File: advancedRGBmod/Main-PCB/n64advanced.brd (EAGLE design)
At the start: 64.5 x 37.7 mm, 112 parts, among them J6 UPS, U1 10CL010YE144, U2 ADV7125/ADV7123, U4 74LVC3G17, U5 S25FLXXXSO8-DUAL, U6 TLV70012DDC, U7 TLV70025DDC

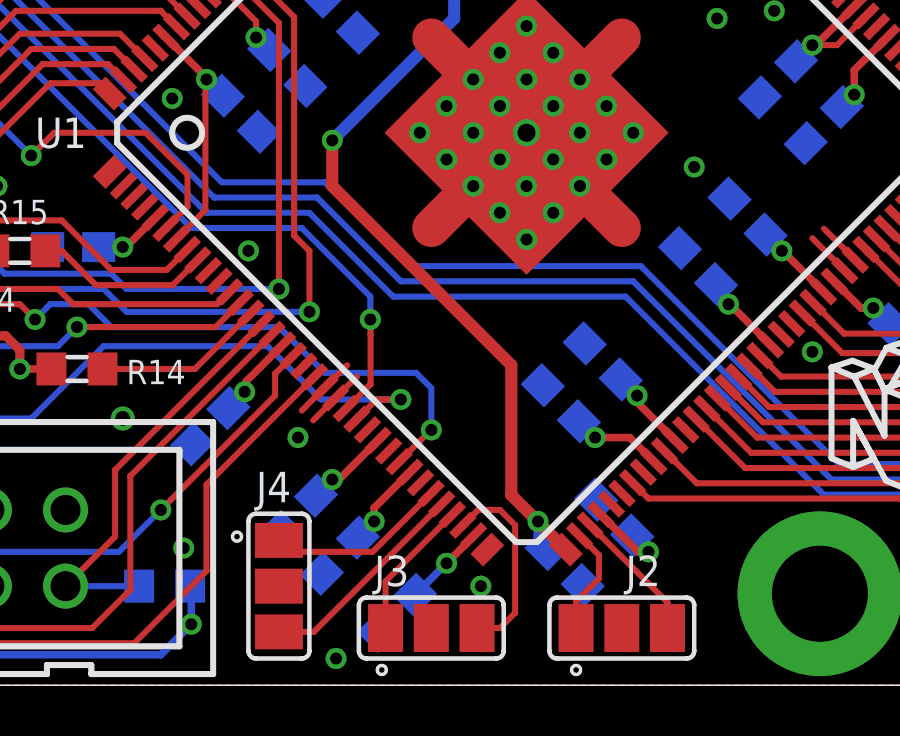
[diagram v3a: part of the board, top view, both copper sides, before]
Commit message: important DRC error fix in PCB design! If you ordered version N64A_20171017 - like I did -, you can unfortunately throw them away :(. There was a design error in the board such that there is a short in an internal plane between VCCDPLL (1.2V) and VCCA (2.5V), which is not easy to fix (fix would need some trace cuts and rewiring)
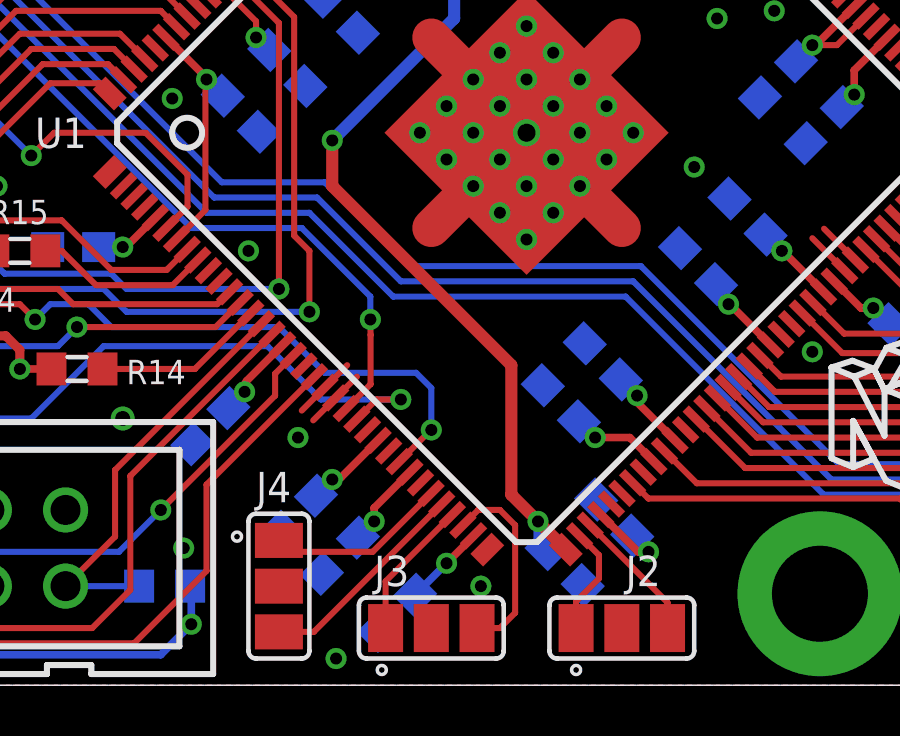
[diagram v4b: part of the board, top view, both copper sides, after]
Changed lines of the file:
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@@
 <layer number="13" name="Route13" color="4" fill="5" visible="no" active="no"/>
 <layer number="14" name="Route14" color="1" fill="6" visible="no" active="no"/>
-<layer number="15" name="Route15" color="4" fill="6" visible="no" active="yes"/>
+<layer number="15" name="Route15" color="4" fill="6" visible="yes" active="yes"/>
 <layer number="16" name="Bottom" color="1" fill="1" visible="yes" active="yes"/>
 <layer number="17" name="Pads" color="2" fill="1" visible="yes" active="yes"/>
@@
 <wire x1="28.702" y1="33.401" x2="28.702" y2="22.225" width="0.4064" layer="16"/>
 <via x="24.638" y="18.161" extent="1-16" drill="0.4"/>
-<wire x1="30.607" y1="6.336496875" x2="32.423146875" y2="4.52035" width="0.4064" layer="1"/>
 <via x="31.496" y="5.461" extent="1-16" drill="0.4"/>
-<wire x1="32.56365" y1="4.52035" x2="32.423146875" y2="4.52035" width="0.254" layer="1"/>
+<wire x1="32.423146875" y1="4.52035" x2="32.56365" y2="4.52035" width="0.254" layer="1"/>
 <wire x1="28.702" y1="22.225" x2="24.638" y2="18.161" width="0.4064" layer="16"/>
 <wire x1="24.638" y1="18.161" x2="24.638" y2="16.637" width="0.4064" layer="1"/>
 <contactref element="U1" pad="37"/>
 <contactref element="U1" pad="109"/>
-<wire x1="24.638" y1="16.637" x2="30.607" y2="10.668" width="0.4064" layer="1"/>
-<wire x1="30.607" y1="10.668" x2="30.607" y2="6.336496875" width="0.4064" layer="1"/>
+<wire x1="30.607" y1="10.668" x2="24.638" y2="16.637" width="0.4064" layer="1"/>
 <wire x1="31.783959375" y1="4.538040625" x2="31.496" y2="4.826" width="0.3048" layer="16"/>
 <wire x1="31.496" y1="4.826" x2="31.496" y2="5.461" width="0.3048" layer="16"/>
-<wire x1="31.783959375" y1="4.538040625" x2="32.423146875" y2="4.52035" width="0" layer="19" extent="1-16"/>
+<wire x1="30.607" y1="6.35" x2="31.496" y2="5.461" width="0.4064" layer="1"/>
+<wire x1="30.607" y1="6.35" x2="30.607" y2="10.668" width="0.4064" layer="1"/>
+<wire x1="31.496" y1="5.461" x2="32.423146875" y2="4.533853125" width="0.4064" layer="1"/>
+<wire x1="32.423146875" y1="4.533853125" x2="32.423146875" y2="4.52035" width="0.4064" layer="1"/>
 </signal>
 <signal name="VCCIO">
@@
 <wire x1="28.448" y1="4.064" x2="27.051" y2="2.667" width="0.254" layer="15"/>
 <wire x1="45.212" y1="21.336" x2="45.212" y2="12.7" width="0.4064" layer="15"/>
-<wire x1="45.212" y1="12.7" x2="38.354" y2="5.842" width="0.4064" layer="15"/>
-<wire x1="38.354" y1="5.842" x2="30.226" y2="5.842" width="0.4064" layer="15"/>
-<wire x1="30.226" y1="5.842" x2="28.448" y2="4.064" width="0.4064" layer="15"/>
+<wire x1="45.212" y1="12.7" x2="38.989" y2="6.477" width="0.4064" layer="15"/>
+<wire x1="38.989" y1="6.477" x2="30.861" y2="6.477" width="0.4064" layer="15"/>
+<wire x1="30.861" y1="6.477" x2="28.448" y2="4.064" width="0.4064" layer="15"/>
 <wire x1="27.051" y1="2.667" x2="20.574" y2="2.667" width="0.254" layer="15"/>
 <wire x1="20.574" y1="2.667" x2="19.939" y2="2.032" width="0.254" layer="15"/>

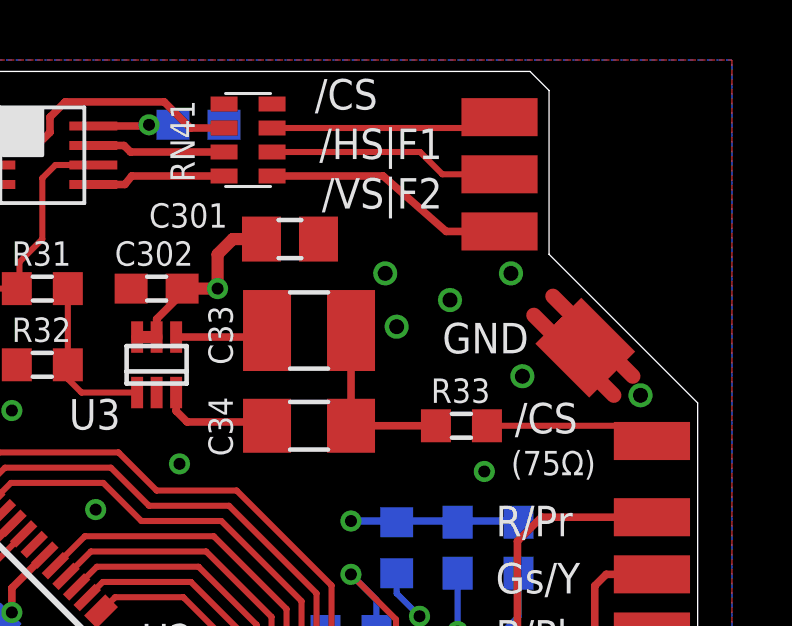
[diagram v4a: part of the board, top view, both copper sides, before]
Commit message: remove separate eagle 7.x version
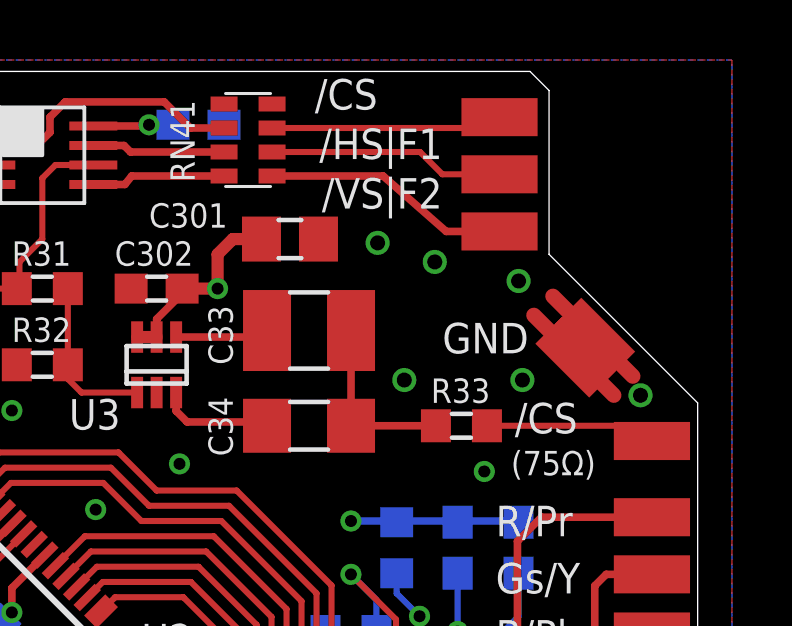
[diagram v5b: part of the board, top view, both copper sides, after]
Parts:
- moved U$1 1.63 mm to (59.7, 27.9)
- moved U$2 1.27 mm to (47.2, 26.9)
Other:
- board text added: "N64A_20171019"
- board text removed: "N64A_20171017"
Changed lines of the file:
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@@
 <circle x="32.766" y="0.508" radius="0.05679375" width="0.3048" layer="25"/>
 <circle x="29.464" y="37.211" radius="0.05679375" width="0.3048" layer="25"/>
-<text x="10.668" y="1.27" size="1.016" layer="26" font="vector" ratio="12" rot="MR0" align="center">N64A_20171017</text>
+<text x="10.668" y="1.27" size="1.016" layer="26" font="vector" ratio="12" rot="MR0" align="center">N64A_20171019</text>
 <wire x1="11.303" y1="30.861" x2="11.303" y2="33.909" width="0.1524" layer="25"/>
 <wire x1="11.303" y1="33.909" x2="12.573" y2="35.179" width="0.1524" layer="25"/>
@@
 <attribute name="OC_NEWARK" value="unknown" x="59.69" y="15.113" size="1.778" layer="27" rot="R270" display="off"/>
 </element>
-<element name="U8" library="crystal-geyer_V1_0" library_urn="urn:adsk.eagle:library:203" package="3.2X2.5_KXO-V96" package3d_urn="urn:adsk.eagle:package:11941/1" value="" x="7.62" y="10.795" smashed="yes" rot="R180">
+<element name="U8" library="crystal-geyer_V1_0" package="3.2X2.5_KXO-V96" value="" x="7.62" y="10.795" smashed="yes" rot="R180">
 <attribute name="VALUE" x="9.42" y="13.695" size="1.016" layer="27" rot="R180"/>
 </element>
 <element name="U5" library="cypress" package="SO8-DUAL" value="S25FLXXXSO8-DUAL" x="5.715" y="14.478" smashed="yes" rot="MR90"/>
 <element name="P_GND4" library="wirepad" package="SMD1,27-2,54" value="" x="60.833" y="28.194" smashed="yes" rot="R45"/>
-<element name="U$1" library="logo" library_urn="urn:adsk.eagle:library:264" package="ESD_10.00" value="" x="60.706" y="26.67" rot="MR0"/>
-<element name="U$2" library="logo" library_urn="urn:adsk.eagle:library:264" package="MUELLTONNE_10.00" value="" x="47.244" y="25.654" rot="MR0"/>
+<element name="U$1" library="logo" package="ESD_10.00" value="" x="59.69" y="27.94" rot="MR0"/>
+<element name="U$2" library="logo" package="MUELLTONNE_10.00" value="" x="47.244" y="26.924" rot="MR0"/>
 </elements>
 <signals>
@@
 <via x="63.5" y="15.24" extent="1-16" drill="0.5"/>
 <via x="60.96" y="12.065" extent="1-16" drill="0.5"/>
-<via x="54.483" y="30.988" extent="1-16" drill="0.5"/>
-<via x="56.642" y="30.099" extent="1-16" drill="0.5"/>
+<via x="54.229" y="32.004" extent="1-16" drill="0.5"/>
+<via x="56.134" y="31.369" extent="1-16" drill="0.5"/>
 <via x="62.992" y="26.924" extent="1-16" drill="0.5"/>
-<via x="58.674" y="30.988" extent="1-16" drill="0.5"/>
-<via x="54.864" y="29.21" extent="1-16" drill="0.5"/>
+<via x="58.928" y="30.734" extent="1-16" drill="0.5"/>
+<via x="55.118" y="27.432" extent="1-16" drill="0.5"/>
 <via x="46.99" y="17.78" extent="1-16" drill="0.4"/>
 <via x="55.245" y="0.889" extent="1-16" drill="0.4"/>
@@
 <contactref element="RN23" pad="4"/>
 <contactref element="RN23" pad="3"/>
-<via x="59.055" y="27.559" extent="1-16" drill="0.5"/>
+<via x="59.055" y="27.432" extent="1-16" drill="0.5"/>
 <via x="50.8" y="15.875" extent="1-16" drill="0.4"/>
 <wire x1="49.527684375" y1="8.9177125" x2="49.9397375" y2="8.9431125" width="0.2032" layer="1"/>
@@
 </board>
 </drawing>
-<compatibility>
-<note version="8.2" severity="warning">
-Since Version 8.2, EAGLE supports online libraries. The ids
-of those online libraries will not be understood (or retained)
-with this version.
-</note>
-<note version="8.3" severity="warning">
-Since Version 8.3, EAGLE supports URNs for individual library
-assets (packages, symbols, and devices). The URNs of those assets
-will not be understood (or retained) with this version.
-</note>
-<note version="8.3" severity="warning">
-Since Version 8.3, EAGLE supports the association of 3D packages
-with devices in libraries, schematics, and board files. Those 3D
-packages will not be understood (or retained) with this version.
-</note>
-</compatibility>
 </eagle>
